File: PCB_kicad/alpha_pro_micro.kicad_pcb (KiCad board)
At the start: 2 copper layers, 192.9 x 59.5 mm, 72 parts, among them J1 Conn_01x03, J2 Conn_01x01_Female, J3 Conn_01x01_Female, J4 Conn_01x01_Female, J5 Conn_01x01_Female, J6 Conn_01x01_Female, J7 Conn_01x01_Female, J8 Conn_01x01_Female, J9 Conn_01x01_Female, K1 KEYSW, K10 KEYSW, K11 KEYSW, K12 KEYSW, K13 KEYSW, K14 KEYSW, K15 KEYSW, K16 KEYSW, K17 KEYSW, K18 KEYSW, K19 KEYSW, K2 KEYSW, K20 KEYSW, K21 KEYSW, K22 KEYSW, K23 KEYSW, K24 KEYSW, K25 KEYSW, K26 KEYSW, K27 KEYSW, K28 KEYSW, K3 KEYSW, K4 KEYSW, K5 KEYSW, K6 KEYSW, K7 KEYSW, K8 KEYSW, K9 KEYSW, SW1 SW_Push, U1 ProMicro

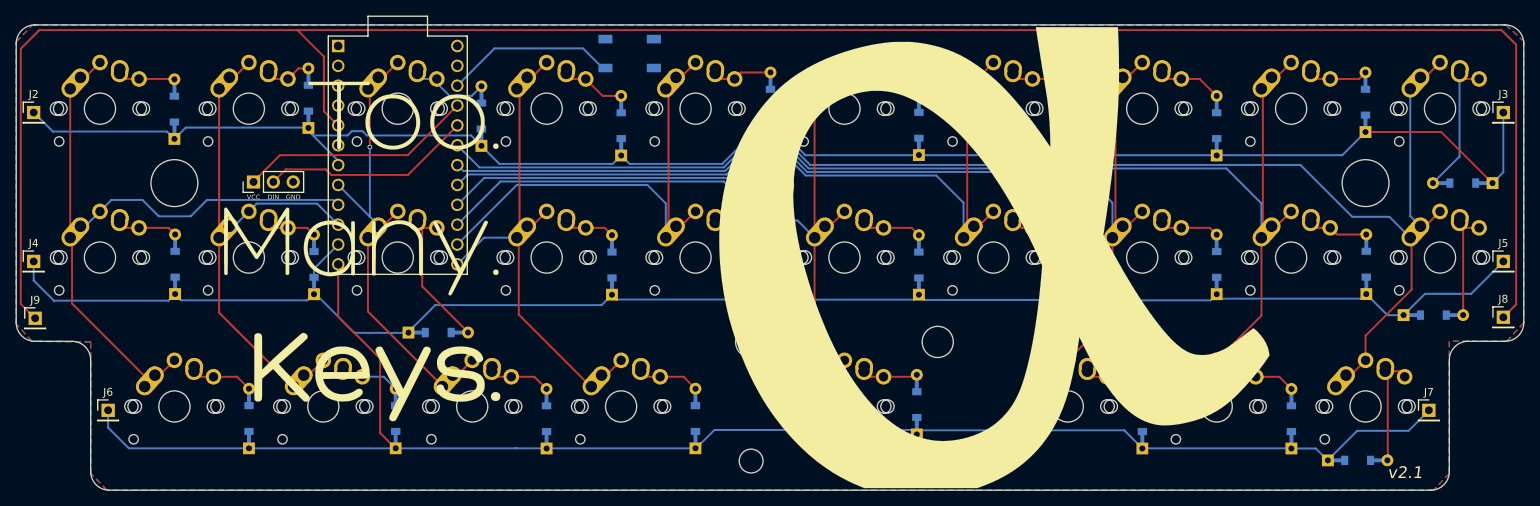
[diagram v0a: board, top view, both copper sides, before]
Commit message: removed tmo28 breakouts
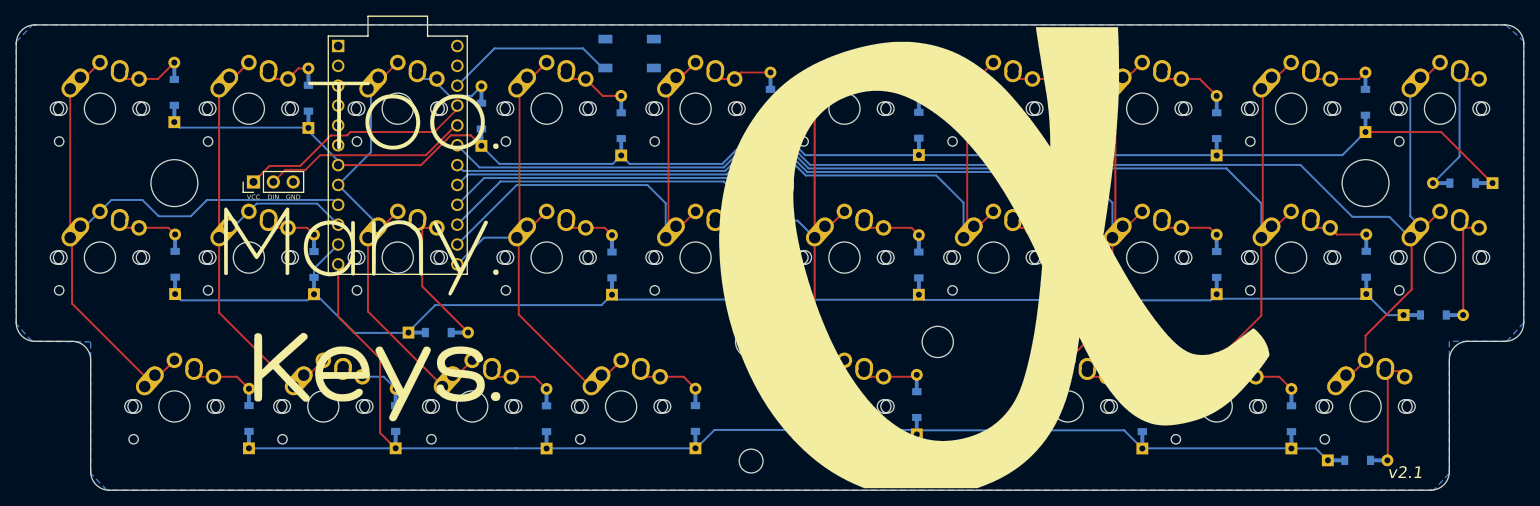
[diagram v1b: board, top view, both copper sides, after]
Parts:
- removed J2, J3, J4, J5, J6, J7, J8, J9: Conn_01x01_Female, Connector_PinHeader_2.54mm:PinHeader_1x01_P2.54mm_Vertical
- moved D1 2.14 mm to (85.7, 107.5)
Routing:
- net /col_tmo: track 278.2 -> 0.00 mm
- net /row1: track 210.6 -> 173.1 mm
- net /row2: track 204.4 -> 167.5 mm
- net /row0: track 212.4 -> 181.0 mm
- net /col2: track 55.1 -> 52.6 mm, vias 1 -> 0
- net Net-(D1-Pad2): track 7.48 -> 8.31 mm
- net RGB: track 27.1 -> 26.5 mm
- removed copper zone on F.Cu, net GND
